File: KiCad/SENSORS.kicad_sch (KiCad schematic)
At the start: 9 parts, among them IC1 A3144EUA, J25 Screw_Terminal_01x02, U123 TMP102xxDRL

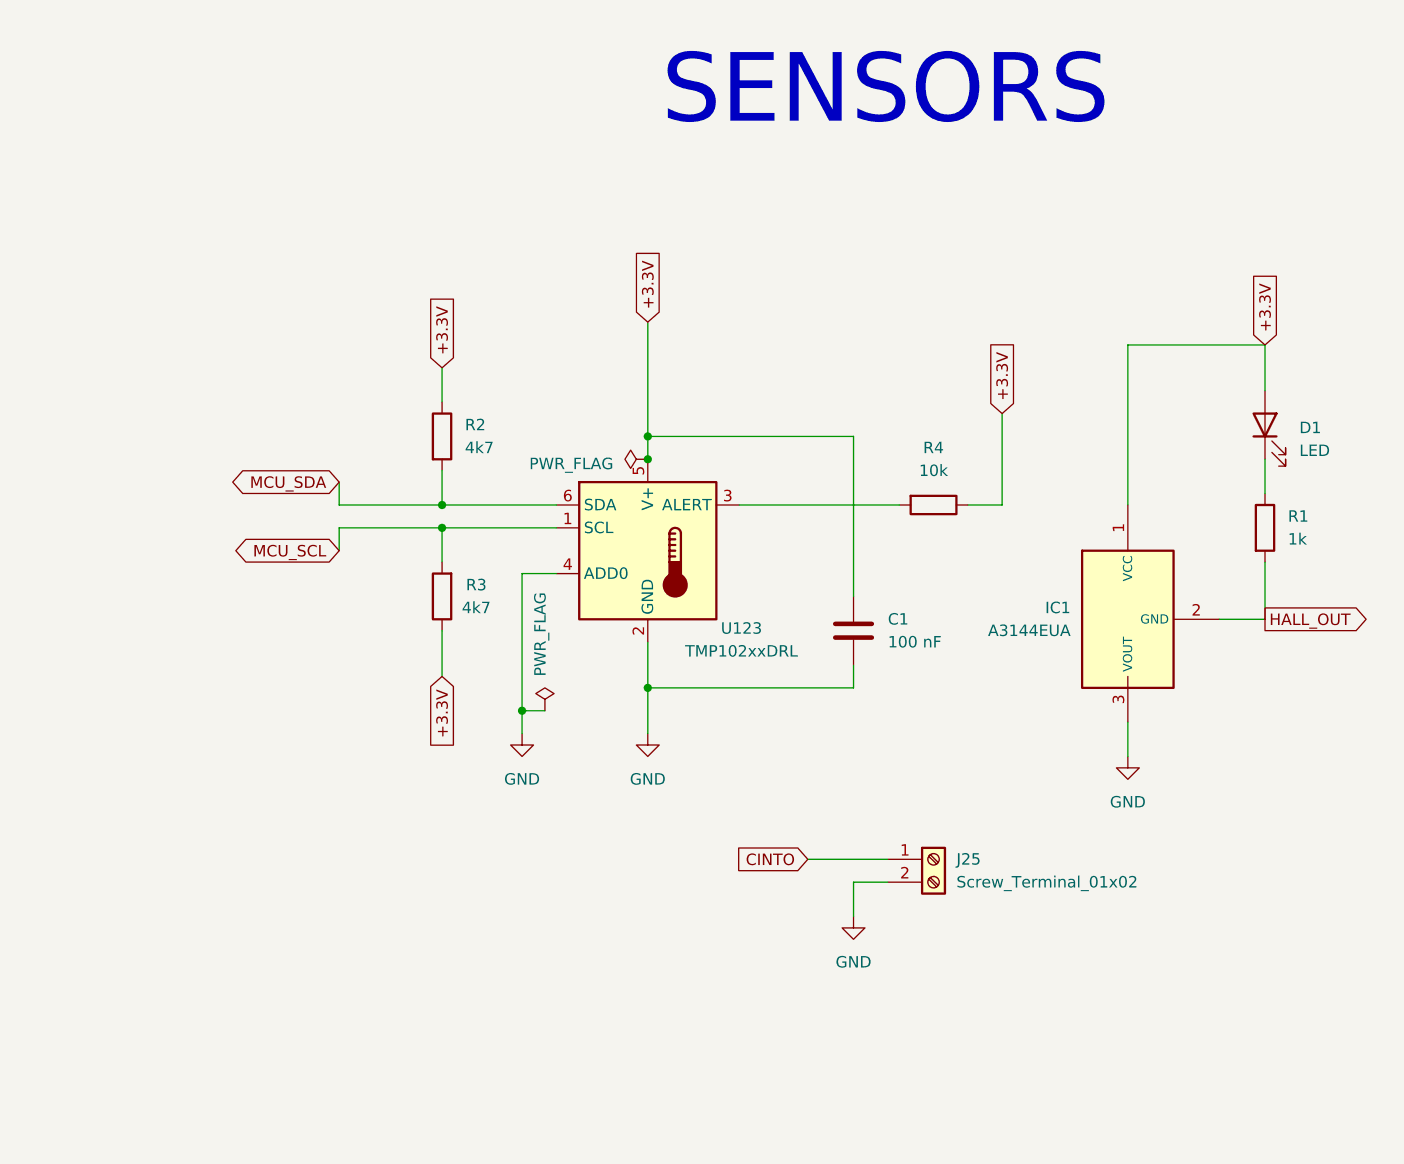
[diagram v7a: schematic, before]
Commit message: Modificació d'errors varis
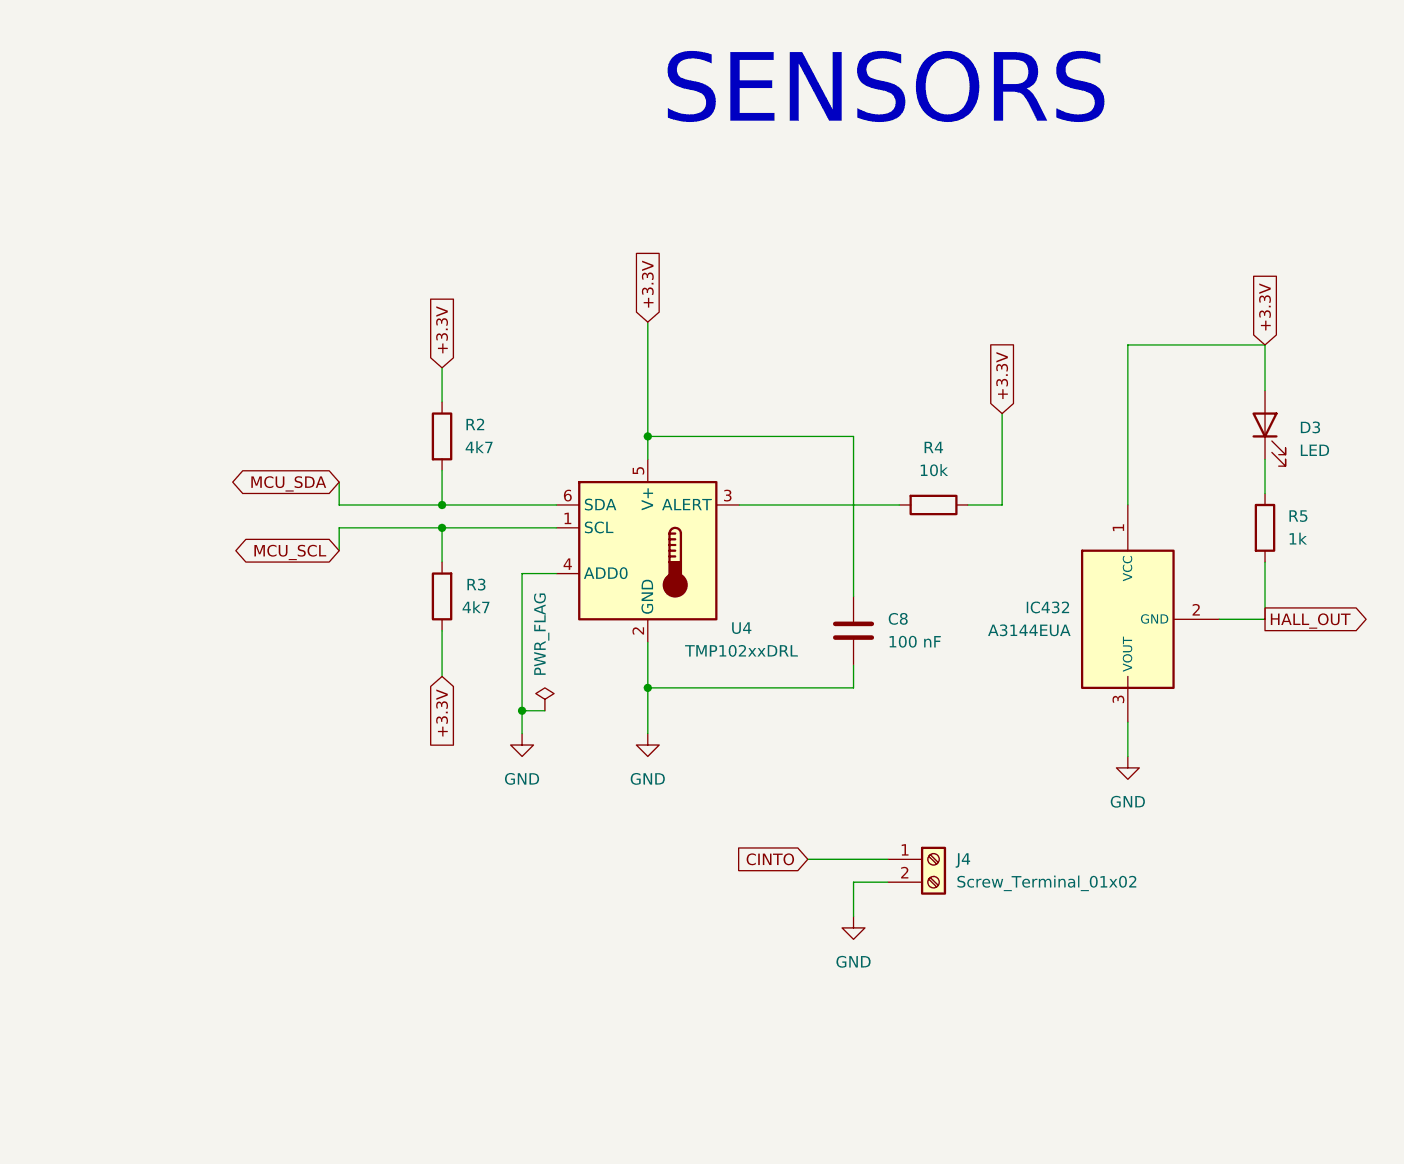
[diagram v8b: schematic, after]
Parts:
- renumbered C1 to C8, D1 to D3, IC1 to IC432, J25 to J4, R1 to R5, U123 to U4
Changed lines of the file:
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@@
-		(color 0 0 0 0)
-	)
-	(junction
-		(at 123.19 96.52)
-		(diameter 0)
 		(color 0 0 0 0)
 	)
@@
 		(dnp no)
 		(fields_autoplaced yes)
-		(property "Reference" "IC1"
+		(property "Reference" "IC432"
 			(at 170.18 113.0299 0)
 			(effects
@@
 				(path "/264905d4-7c45-4183-babb-a5b2177ba886"
 					(reference "IC1")
+					(unit 1)
+				)
+			)
+			(project "SEIENTS_EDD"
+				(path "/b6401b4f-5426-49b8-bb2e-8ecdb19989ef/e4bd2572-b2cc-4f8d-9ea8-3fa488d49274"
+					(reference "IC432")
 					(unit 1)
 				)
@@
 		(dnp no)
 		(fields_autoplaced yes)
-		(property "Reference" "C1"
+		(property "Reference" "C8"
 			(at 149.86 114.2999 0)
 			(effects
@@
 		(dnp no)
 		(fields_autoplaced yes)
-		(property "Reference" "J25"
+		(property "Reference" "J4"
 			(at 157.48 140.9699 0)
 			(effects
@@
 		(on_board yes)
 		(dnp no)
-		(property "Reference" "U123"
+		(property "Reference" "U4"
 			(at 133.604 115.316 0)
 			(effects
@@
 		(dnp no)
 		(fields_autoplaced yes)
-		(property "Reference" "D1"
+		(property "Reference" "D3"
 			(at 195.58 93.0274 90)
 			(effects
@@
 		(dnp no)
 		(fields_autoplaced yes)
-		(property "Reference" "R1"
+		(property "Reference" "R5"
 			(at 194.31 102.8699 0)
 			(effects
@@
 		(dnp no)
 		(fields_autoplaced yes)
-		(property "Reference" "#PWR01"
+		(property "Reference" "#PWR012"
 			(at 109.22 133.35 0)
 			(effects
@@
 		(dnp no)
 		(fields_autoplaced yes)
-		(property "Reference" "#PWR03"
+		(property "Reference" "#PWR014"
 			(at 176.53 135.89 0)
 			(effects
@@
 				(path "/b6401b4f-5426-49b8-bb2e-8ecdb19989ef/e4bd2572-b2cc-4f8d-9ea8-3fa488d49274"
 					(reference "#PWR014")
-					(unit 1)
-				)
-			)
-		)
-	)
-	(symbol
-		(lib_id "power:PWR_FLAG")
-		(at 123.19 96.52 90)
-		(unit 1)
-		(exclude_from_sim no)
-		(in_bom yes)
-		(on_board yes)
-		(dnp no)
-		(property "Reference" "#FLG01"
-			(at 121.285 96.52 0)
-			(effects
-				(font
-					(size 1.27 1.27)
-				)
-				(hide yes)
-			)
-		)
-		(property "Value" "PWR_FLAG"
-			(at 119.38 97.028 90)
-			(effects
-				(font
-					(size 1.27 1.27)
-				)
-				(justify left)
-			)
-		)
-		(property "Footprint" ""
-			(at 123.19 96.52 0)
-			(effects
-				(font
-					(size 1.27 1.27)
-				)
-				(hide yes)
-			)
-		)
-		(property "Datasheet" "~"
-			(at 123.19 96.52 0)
-			(effects
-				(font
-					(size 1.27 1.27)
-				)
-				(hide yes)
-			)
-		)
-		(property "Description" "Special symbol for telling ERC where power comes from"
-			(at 123.19 96.52 0)
-			(effects
-				(font
-					(size 1.27 1.27)
-				)
-				(hide yes)
-			)
-		)
-		(pin "1"
-		)
-		(instances
-			(project ""
-				(path "/264905d4-7c45-4183-babb-a5b2177ba886"
-					(reference "#FLG01")
 					(unit 1)
 				)
@@
 		(dnp no)
 		(fields_autoplaced yes)
-		(property "Reference" "#PWR02"
+		(property "Reference" "#PWR013"
 			(at 123.19 133.35 0)
 			(effects
@@
 		(on_board yes)
 		(dnp no)
-		(property "Reference" "#FLG02"
+		(property "Reference" "#FLG0105"
 			(at 111.76 122.555 0)
 			(effects
@@
 				(path "/264905d4-7c45-4183-babb-a5b2177ba886"
 					(reference "#FLG02")
+					(unit 1)
+				)
+			)
+			(project "SEIENTS_EDD"
+				(path "/b6401b4f-5426-49b8-bb2e-8ecdb19989ef/e4bd2572-b2cc-4f8d-9ea8-3fa488d49274"
+					(reference "#FLG0105")
 					(unit 1)
 				)
@@
 		(dnp no)
 		(fields_autoplaced yes)
-		(property "Reference" "#PWR04"
+		(property "Reference" "#PWR038"
 			(at 146.05 153.67 0)
 			(effects
